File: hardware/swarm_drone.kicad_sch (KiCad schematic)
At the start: 6 parts

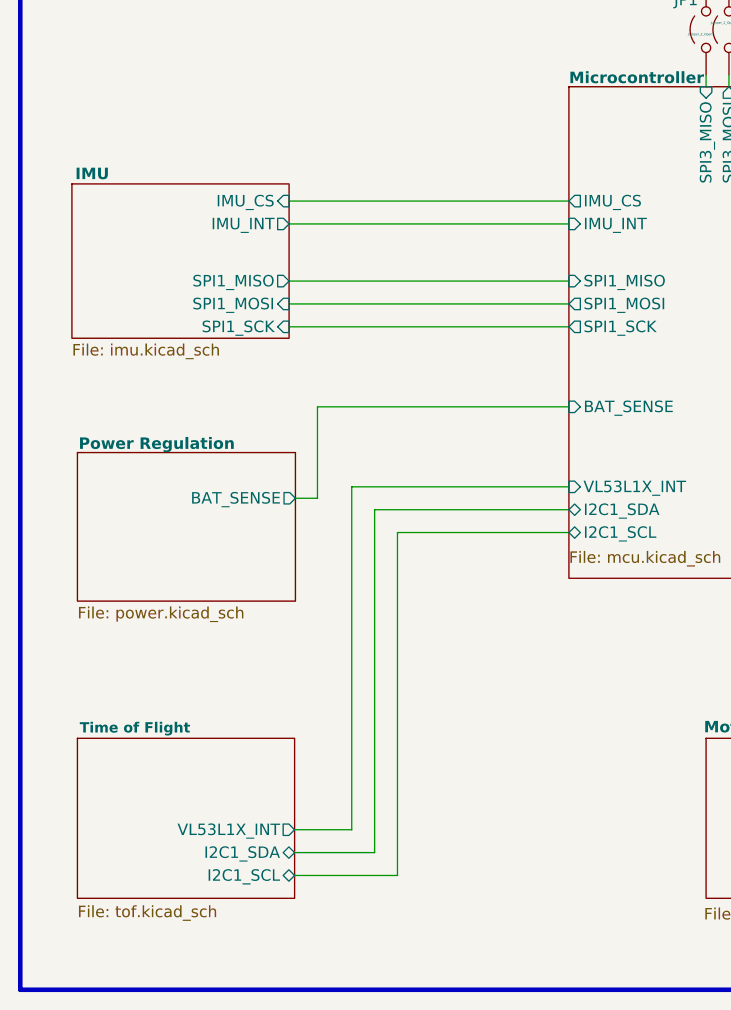
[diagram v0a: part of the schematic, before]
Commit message: feat(kicad): Cleared ERC errors and assigned footprints for all parts
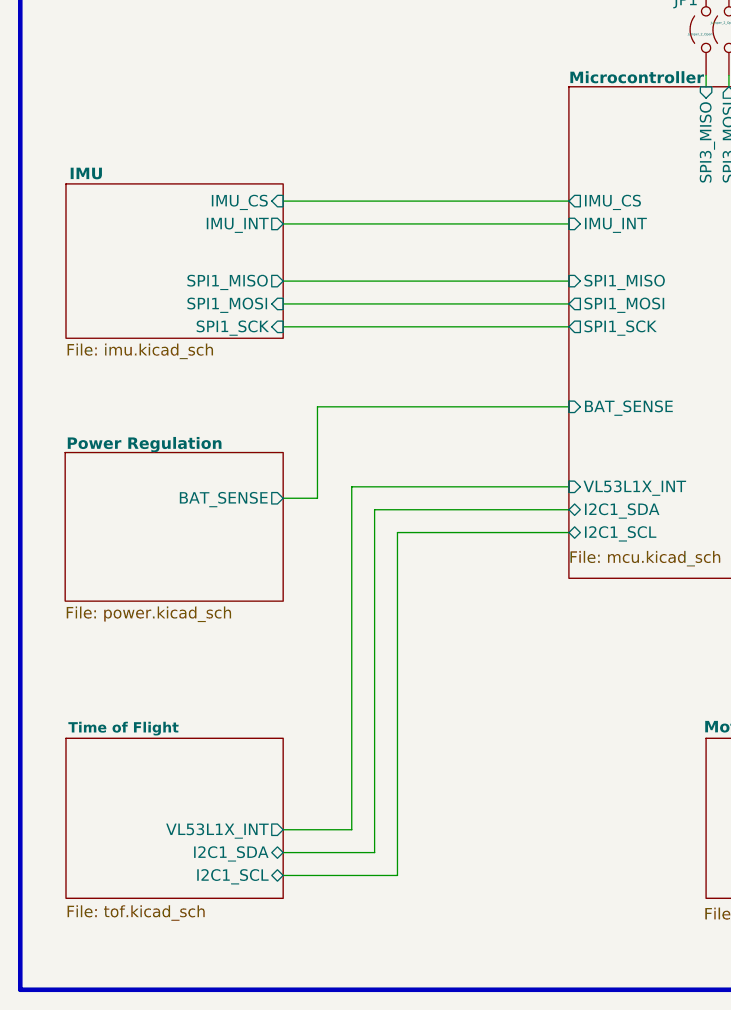
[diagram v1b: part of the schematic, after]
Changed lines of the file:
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@@
 	(wire
 		(pts
-			(xy 96.52 144.78) (xy 90.17 144.78)
+			(xy 96.52 144.78) (xy 88.9 144.78)
 		)
 		(stroke
@@
 	(wire
 		(pts
-			(xy 89.5567 86.36) (xy 120.65 86.36)
+			(xy 88.9 86.36) (xy 120.65 86.36)
 		)
 		(stroke
@@
 	(wire
 		(pts
-			(xy 90.17 149.86) (xy 101.6 149.86)
+			(xy 88.9 149.86) (xy 101.6 149.86)
 		)
 		(stroke
@@
 	(wire
 		(pts
-			(xy 89.5567 83.82) (xy 120.65 83.82)
+			(xy 88.9 83.82) (xy 120.65 83.82)
 		)
 		(stroke
@@
 	(wire
 		(pts
-			(xy 99.06 147.32) (xy 90.17 147.32)
+			(xy 99.06 147.32) (xy 88.9 147.32)
 		)
 		(stroke
@@
 	(wire
 		(pts
-			(xy 89.5567 88.9) (xy 120.65 88.9)
+			(xy 88.9 88.9) (xy 120.65 88.9)
 		)
 		(stroke
@@
 	(wire
 		(pts
-			(xy 89.5567 74.93) (xy 120.65 74.93)
+			(xy 88.9 74.93) (xy 120.65 74.93)
 		)
 		(stroke
@@
 	(wire
 		(pts
-			(xy 90.263 107.95) (xy 92.71 107.95)
-		)
-		(stroke
-			(width 0)
-			(type default)
-		)
-	)
-	(wire
-		(pts
-			(xy 89.5567 77.47) (xy 120.65 77.47)
+			(xy 88.9 107.95) (xy 92.71 107.95)
+		)
+		(stroke
+			(width 0)
+			(type default)
+		)
+	)
+	(wire
+		(pts
+			(xy 88.9 77.47) (xy 120.65 77.47)
 		)
 		(stroke
@@
 	)
 	(sheet
-		(at 66.04 102.87)
+		(at 64.677 102.87)
 		(size 24.223 16.51)
 		(exclude_from_sim no)
@@
 		)
 		(property "Sheetname" "Power Regulation"
-			(at 66.167 102.616 0)
+			(at 64.804 102.616 0)
 			(show_name no)
 			(do_not_autoplace no)
@@
 		)
 		(property "Sheetfile" "power.kicad_sch"
-			(at 66.04 119.9646 0)
+			(at 64.677 119.9646 0)
 			(show_name no)
 			(do_not_autoplace no)
@@
 		)
 		(pin "BAT_SENSE" output
-			(at 90.263 107.95 0)
+			(at 88.9 107.95 0)
 			(effects
 				(font
@@
 	)
 	(sheet
-		(at 66.04 134.62)
+		(at 64.77 134.62)
 		(size 24.13 17.78)
 		(exclude_from_sim no)
@@
 		)
 		(property "Sheetname" "Time of Flight"
-			(at 66.294 134.112 0)
+			(at 65.024 134.112 0)
 			(show_name no)
 			(do_not_autoplace no)
@@
 		)
 		(property "Sheetfile" "tof.kicad_sch"
-			(at 66.04 153.162 0)
+			(at 64.77 153.162 0)
 			(show_name no)
 			(do_not_autoplace no)
@@
 		)
 		(pin "I2C1_SCL" bidirectional
-			(at 90.17 149.86 0)
+			(at 88.9 149.86 0)
 			(effects
 				(font
@@
 		)
 		(pin "I2C1_SDA" bidirectional
-			(at 90.17 147.32 0)
+			(at 88.9 147.32 0)
 			(effects
 				(font
@@
 		)
 		(pin "VL53L1X_INT" output
-			(at 90.17 144.78 0)
+			(at 88.9 144.78 0)
 			(effects
 				(font
@@
 	)
 	(sheet
-		(at 65.4267 73.025)
+		(at 64.77 73.025)
 		(size 24.13 17.145)
 		(exclude_from_sim no)
@@
 		)
 		(property "Sheetname" "IMU"
-			(at 65.786 72.644 0)
+			(at 65.1293 72.644 0)
 			(show_name no)
 			(do_not_autoplace no)
@@
 		)
 		(property "Sheetfile" "imu.kicad_sch"
-			(at 65.4267 90.7546 0)
+			(at 64.77 90.7546 0)
 			(show_name no)
 			(do_not_autoplace no)
@@
 		)
 		(pin "IMU_CS" input
-			(at 89.5567 74.93 0)
+			(at 88.9 74.93 0)
 			(effects
 				(font
@@
 		)
 		(pin "IMU_INT" output
-			(at 89.5567 77.47 0)
+			(at 88.9 77.47 0)
 			(effects
 				(font
@@
 		)
 		(pin "SPI1_MOSI" input
-			(at 89.5567 86.36 0)
+			(at 88.9 86.36 0)
 			(effects
 				(font
@@
 		)
 		(pin "SPI1_MISO" output
-			(at 89.5567 83.82 0)
+			(at 88.9 83.82 0)
 			(effects
 				(font
@@
 		)
 		(pin "SPI1_SCK" input
-			(at 89.5567 88.9 0)
-			(effects
-				(font
+			(at 88.9 88.9 0)
+			(effects
+				(font

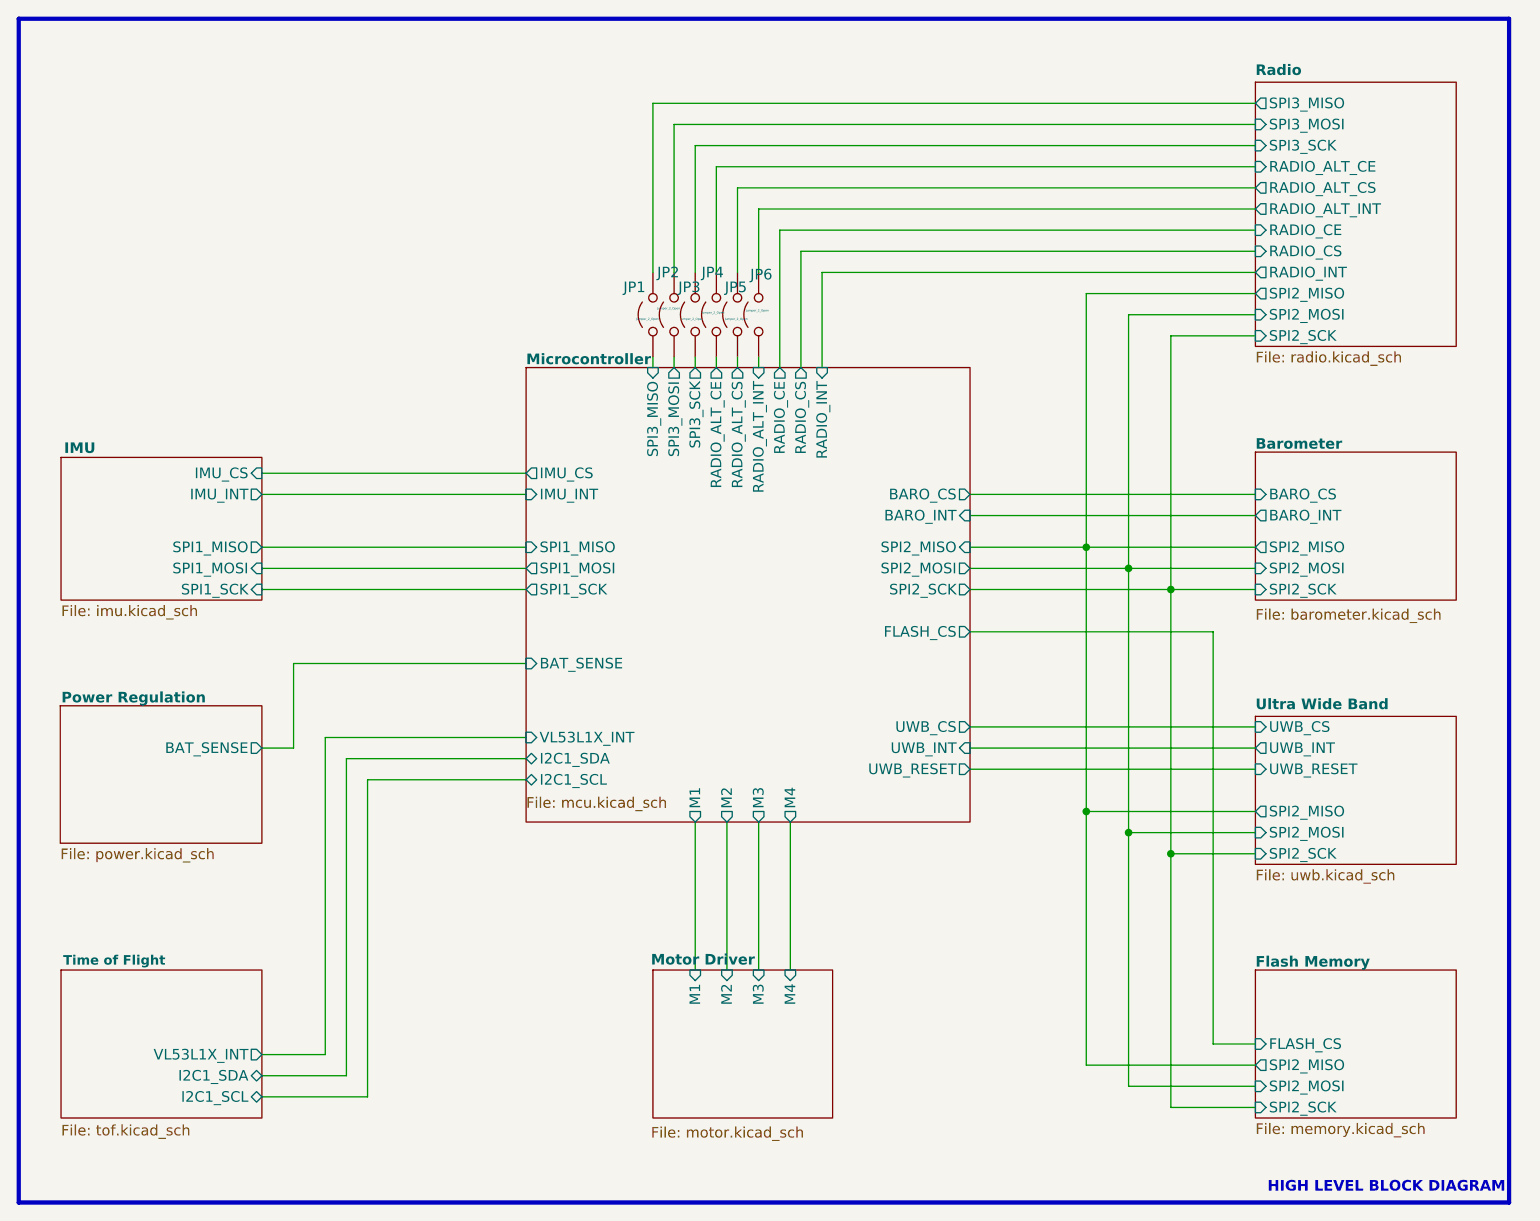
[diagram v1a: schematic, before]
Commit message: feat(kicad): Updated schematic to keep traces shorter on the layout Restarting layout
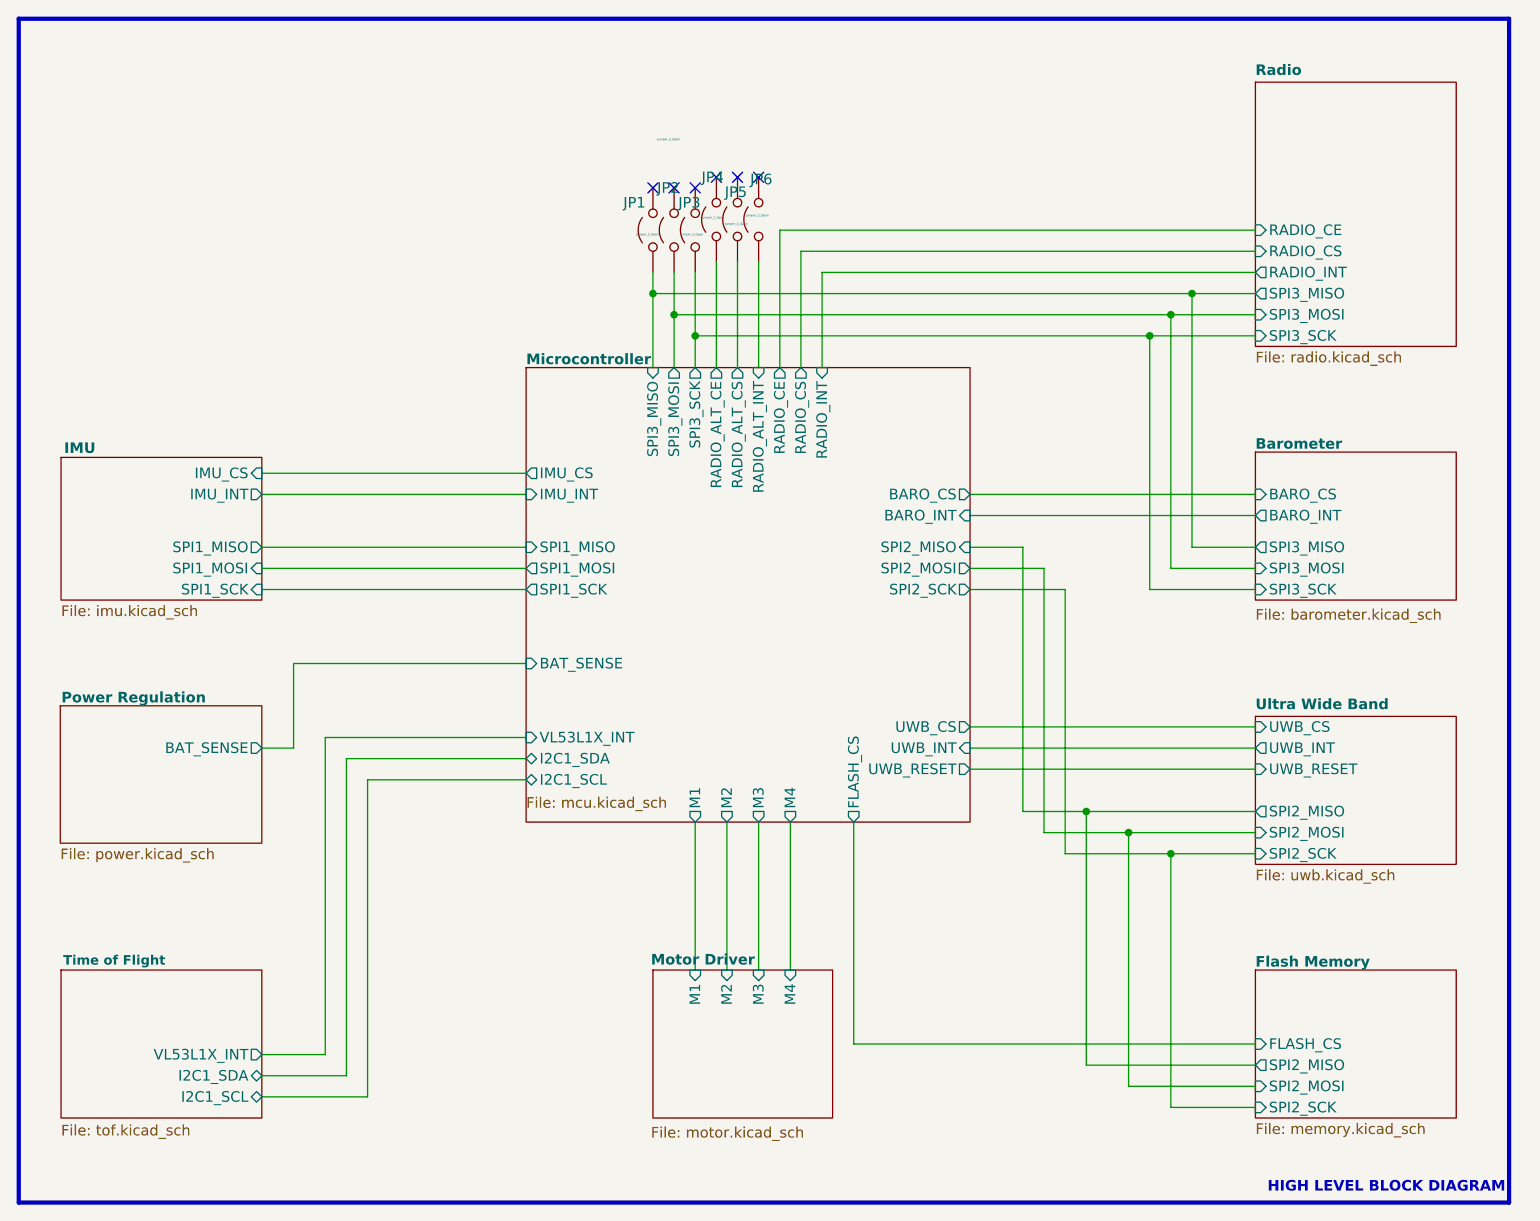
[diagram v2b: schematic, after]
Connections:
- net Microcontroller/SPI3_MISO renamed Barometer/SPI3_MISO
- net Microcontroller/SPI3_MOSI renamed Barometer/SPI3_MOSI
- net Microcontroller/SPI3_SCK renamed Barometer/SPI3_SCK
- net Radio/RADIO_ALT_CE: no longer names the net of JP4.2 (B)
- net Radio/RADIO_ALT_CS: no longer names the net of JP5.2 (B)
- net Radio/RADIO_ALT_INT: no longer names the net of JP6.2 (B)
- net Radio/SPI3_MISO: no longer names the net of JP1.2 (B)
- net Radio/SPI3_MOSI: no longer names the net of JP2.2 (B)
- net Radio/SPI3_SCK: no longer names the net of JP3.2 (B)
- no-connect marks 0 -> 6
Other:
- sheet Barometer ports: added SPI3_MISO, SPI3_MOSI, SPI3_SCK; removed SPI2_MISO, SPI2_MOSI, SPI2_SCK
- sheet Radio ports: added none; removed RADIO_ALT_CE, RADIO_ALT_CS, RADIO_ALT_INT, SPI2_MISO, SPI2_MOSI, SPI2_SCK
- moved on the sheet: JP1, JP2, JP3, JP4, JP5, JP6

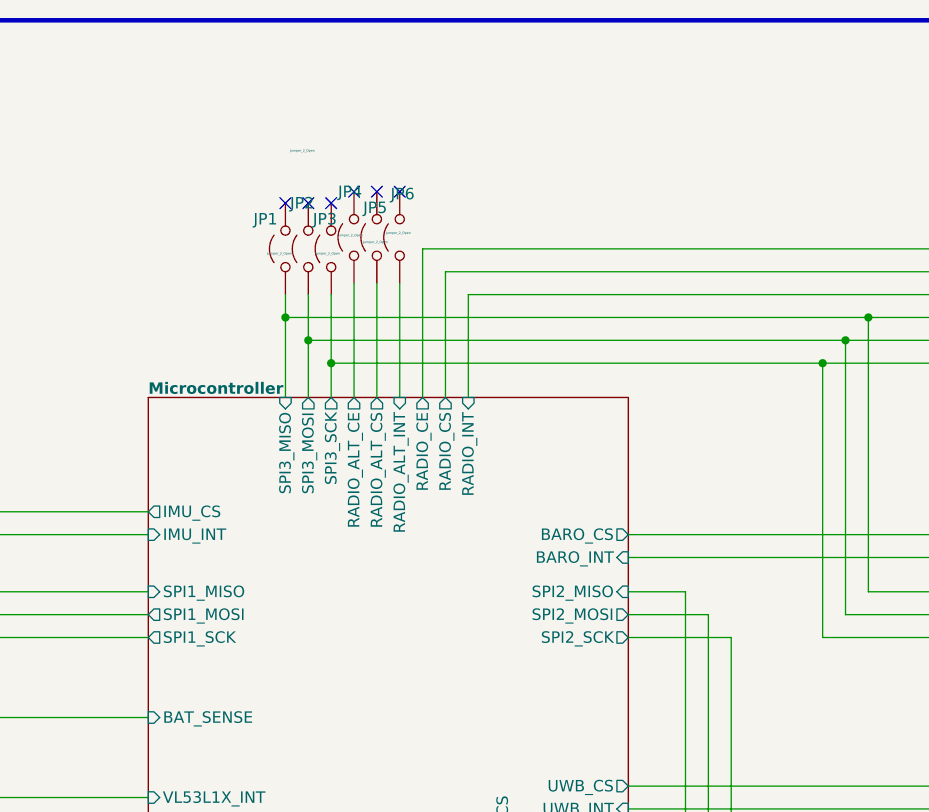
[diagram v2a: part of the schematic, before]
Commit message: feat(kicad): Rerouted board and changed nets to provide ease in routing
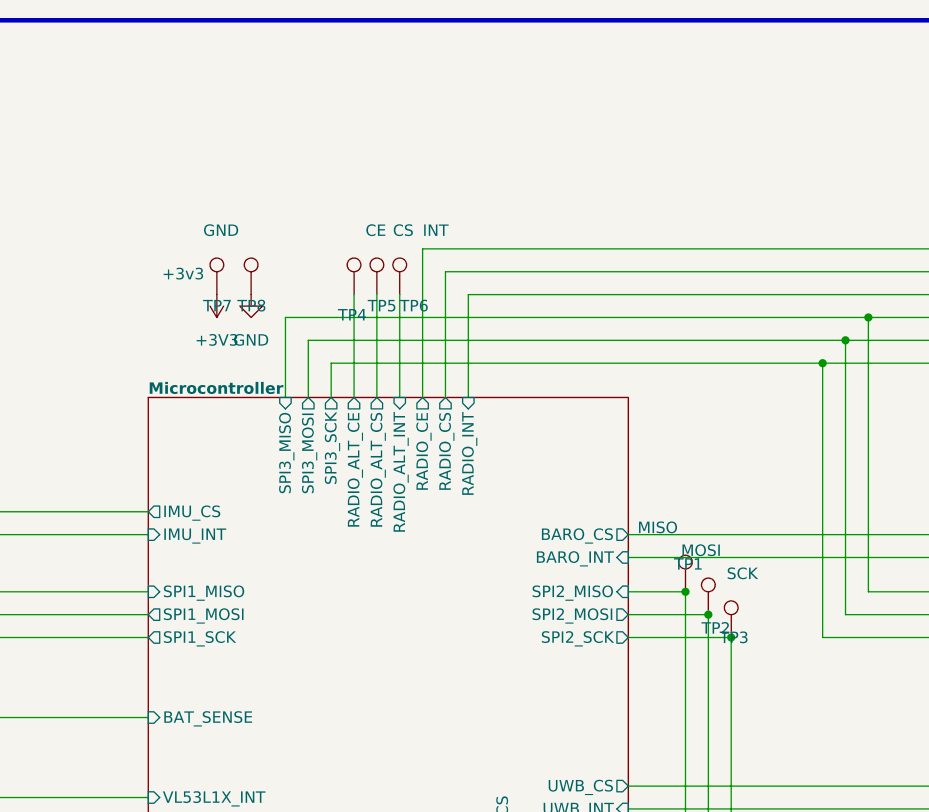
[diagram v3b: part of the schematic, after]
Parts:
- removed JP1, JP2, JP3, JP4, JP5, JP6: Jumper_2_Open, Jumper:SolderJumper-2_P1.3mm_Open_RoundedPad1.0x1.5mm, symbol Jumper:Jumper_2_Open
- added TP1: MISO, TestPoint:TestPoint_Pad_1.0x1.0mm, symbol Connector:TestPoint
- added TP2: MOSI, TestPoint:TestPoint_Pad_1.0x1.0mm, symbol Connector:TestPoint
- added TP3: SCK, TestPoint:TestPoint_Pad_1.0x1.0mm, symbol Connector:TestPoint
- added TP4: CE, TestPoint:TestPoint_Pad_1.0x1.0mm, symbol Connector:TestPoint
- added TP5: CS, TestPoint:TestPoint_Pad_1.0x1.0mm, symbol Connector:TestPoint
- added TP6: INT, TestPoint:TestPoint_Pad_1.0x1.0mm, symbol Connector:TestPoint
- added TP7: +3v3, TestPoint:TestPoint_Pad_1.0x1.0mm, symbol Connector:TestPoint
- added TP8: GND, TestPoint:TestPoint_Pad_1.0x1.0mm, symbol Connector:TestPoint
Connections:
- net Flash Memory/SPI2_MISO: now also TP1.1
- net Flash Memory/SPI2_MOSI: now also TP2.1
- net Flash Memory/SPI2_SCK: now also TP3.1
- net Microcontroller/RADIO_ALT_CE: now also TP4.1
- net Microcontroller/RADIO_ALT_CS: now also TP5.1
- net Microcontroller/RADIO_ALT_INT: now also TP6.1
- new net +3V3: TP7.1
- new net GND: TP8.1
- no-connect marks 6 -> 0
